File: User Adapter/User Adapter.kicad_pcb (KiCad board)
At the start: 2 copper layers, 88.9 x 27.9 mm, 44 parts, among them J1 OHIS_8p8c_Shield, J2 Headphones, J3 Microphone, J4 PTT, J5 Dynamic Mic Bypass, J6 HP or CTIA, Q1 2N3904, SW1 PTT

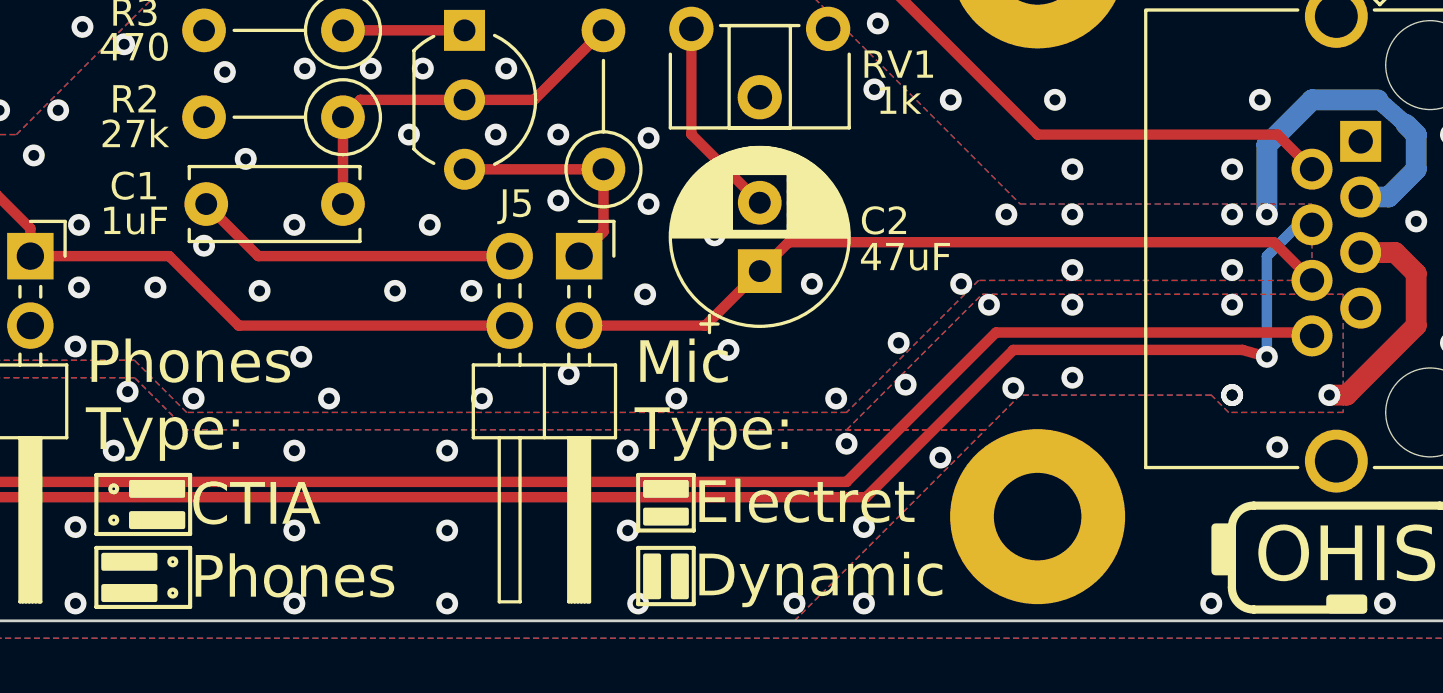
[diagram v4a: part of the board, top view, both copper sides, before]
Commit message: add jumper for mic attenuation. update version on back silkscreen to v1.3
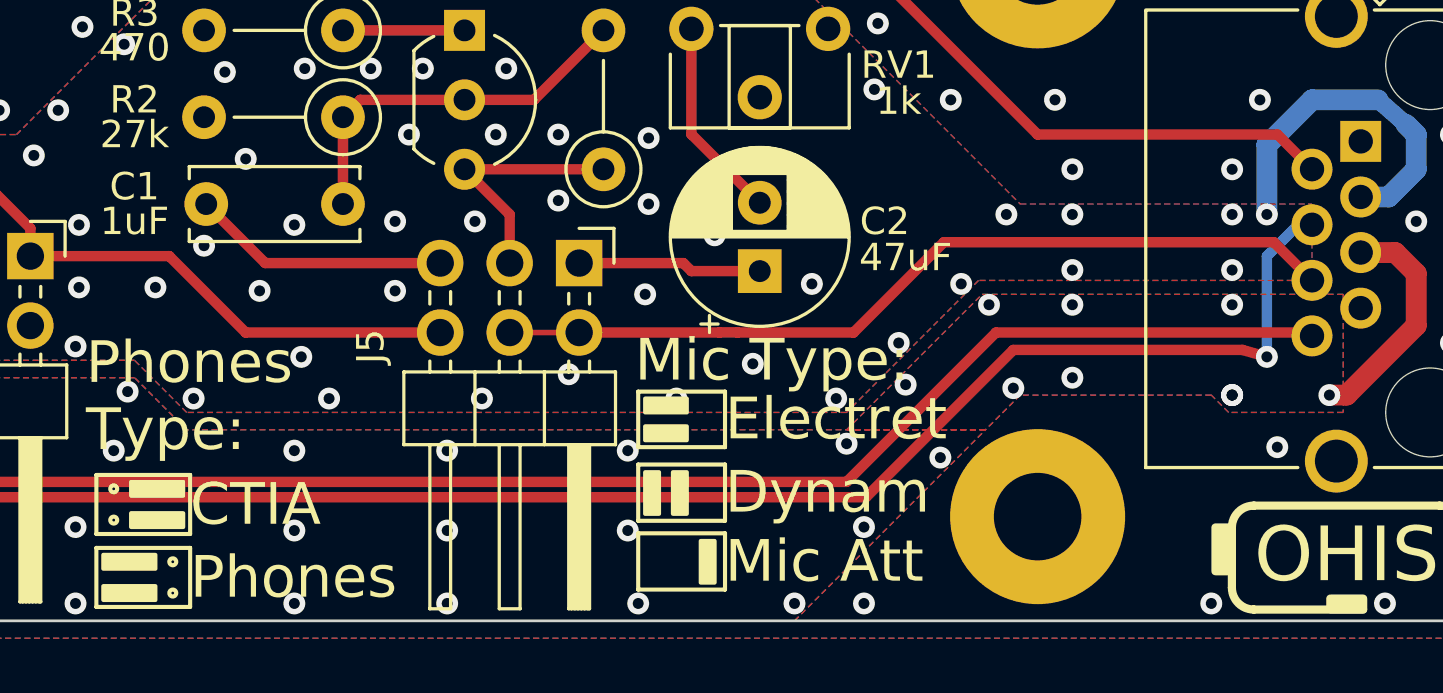
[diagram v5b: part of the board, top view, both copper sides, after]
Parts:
- J5: footprint Connector_PinHeader_2.54mm:PinHeader_2x02_P2.54mm_Horizontal -> Connector_PinHeader_2.54mm:PinHeader_2x03_P2.54mm_Horizontal
- moved J5 0.25 mm to (154.7, 77.1)
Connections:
- C1 pad 1: Net-(J5-Pin_3) -> Net-(J5-Pin_5)
- C2 pad 1: Mic+ -> Net-(J5-Pin_1)
- J5 pad 4: Mic+ 3.5 -> Mic+
- Q1 pad 3: Net-(J5-Pin_1) -> Net-(J5-Pin_3)
- R1 pad 1: Net-(J5-Pin_1) -> Net-(J5-Pin_3)
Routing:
- net Net-(J5-Pin_5): track 0.00 -> 9.45 mm
- net Mic+: track 28.6 -> 31.3 mm
- net Net-(J5-Pin_3): track 11.9 -> 9.19 mm
- net Mic+ 3.5: track 44.2 -> 41.8 mm
- net Net-(J5-Pin_1): track 8.62 -> 6.73 mm
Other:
- board text added: "Dynam"
- board text added: "Mic Att"
- board text added: "OHIS User Adapter v1.3 2024 CC-BY OHIS Working Group"
- board text removed: "Dynamic"
- board text removed: "OHIS User Adapter v1.2a 2024 CC-BY OHIS Working Group"

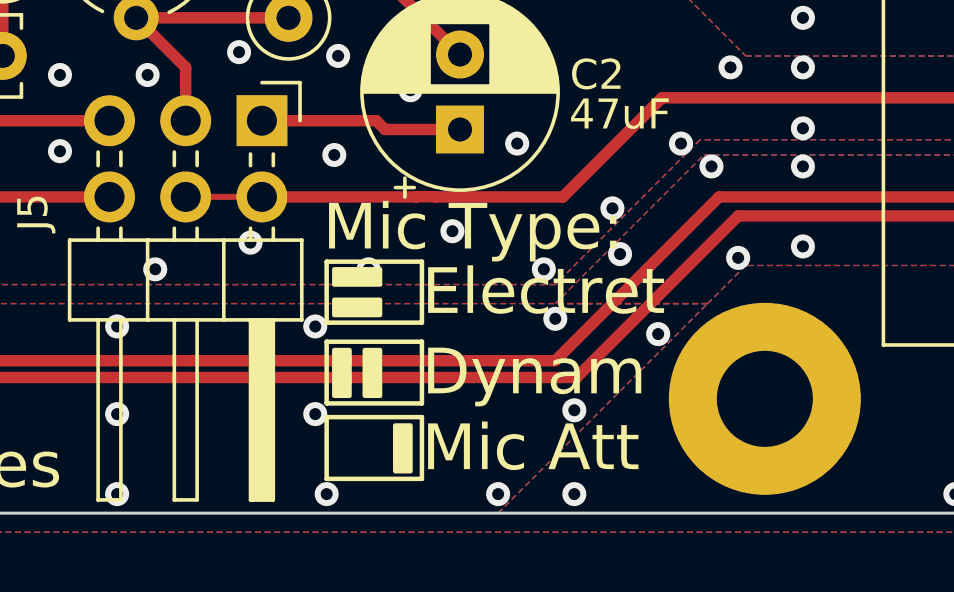
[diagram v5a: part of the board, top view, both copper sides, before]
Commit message: Tweaking a few minor things from the last PR. Added Contributers to README.md
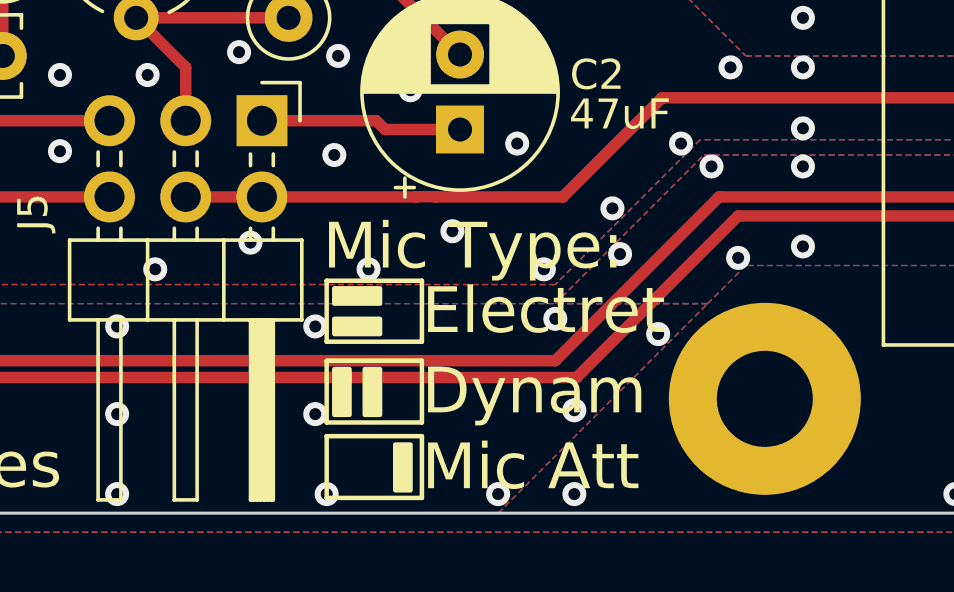
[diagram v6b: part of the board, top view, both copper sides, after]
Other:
- board text added: "OHIS User Adapter v1.3a 2024 CC-BY OHIS Working Group"
- board text removed: "OHIS User Adapter v1.3 2024 CC-BY OHIS Working Group"
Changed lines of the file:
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@@
       (stroke (width 0) (type solid)) (fill solid) (layer "B.SilkS"))
   )
-  (gr_rect (start 159.131 87.249) (end 159.639 88.773)
-    (stroke (width 0.15) (type solid)) (fill solid) (layer "F.SilkS"))
-  (gr_rect (start 157.099 84.7344) (end 157.607 86.2584)
+  (gr_rect (start 159.131 87.884) (end 159.639 89.408)
+    (stroke (width 0.15) (type solid)) (fill solid) (layer "F.SilkS"))
+  (gr_rect (start 157.099 85.3694) (end 157.607 86.8934)
     (stroke (width 0.15) (type solid)) (fill solid) (layer "F.SilkS"))
   (gr_rect (start 137.287 87.757) (end 139.192 88.265)
     (stroke (width 0.15) (type solid)) (fill solid) (layer "F.SilkS"))
-  (gr_rect (start 156.845 84.455) (end 160.02 86.5124)
-    (stroke (width 0.15) (type default)) (fill none) (layer "F.SilkS"))
-  (gr_rect (start 156.845 81.788) (end 160.02 83.82)
-    (stroke (width 0.15) (type default)) (fill none) (layer "F.SilkS"))
-  (gr_rect (start 157.099 83.058) (end 158.623 83.566)
+  (gr_rect (start 156.845 85.09) (end 160.02 87.1474)
+    (stroke (width 0.15) (type default)) (fill none) (layer "F.SilkS"))
+  (gr_rect (start 156.845 82.423) (end 160.02 84.455)
+    (stroke (width 0.15) (type default)) (fill none) (layer "F.SilkS"))
+  (gr_rect (start 157.099 83.693) (end 158.623 84.201)
     (stroke (width 0.15) (type solid)) (fill solid) (layer "F.SilkS"))
   (gr_rect (start 137.287 88.9) (end 139.192 89.408)
@@
   (gr_rect (start 138.303 85.09) (end 140.208 85.598)
     (stroke (width 0.15) (type solid)) (fill solid) (layer "F.SilkS"))
-  (gr_rect (start 156.845 86.9696) (end 160.02 89.027)
+  (gr_rect (start 156.845 87.6046) (end 160.02 89.662)
     (stroke (width 0.15) (type default)) (fill none) (layer "F.SilkS"))
   (gr_circle (center 137.668 86.487) (end 137.668 86.614)
@@
   (gr_circle (center 139.827 88.011) (end 139.827 87.884)
     (stroke (width 0.15) (type default)) (fill none) (layer "F.SilkS"))
-  (gr_rect (start 158.115 84.7344) (end 158.623 86.2584)
+  (gr_rect (start 158.115 85.3694) (end 158.623 86.8934)
     (stroke (width 0.15) (type solid)) (fill solid) (layer "F.SilkS"))
   (gr_rect (start 137.033 87.503) (end 140.462 89.662)
@@
   (gr_rect (start 137.033 84.836) (end 140.462 86.995)
     (stroke (width 0.15) (type default)) (fill none) (layer "F.SilkS"))
-  (gr_rect (start 157.099 82.042) (end 158.623 82.55)
+  (gr_rect (start 157.099 82.677) (end 158.623 83.185)
     (stroke (width 0.15) (type solid)) (fill solid) (layer "F.SilkS"))
   (gr_rect (start 101.6 62.23) (end 190.5 90.17)
@@
     (effects (font (size 1.27 1.27) (thickness 0.1905)) (justify left mirror))
   )
-  (gr_text "OHIS User Adapter v1.3\n2024 CC-BY OHIS Working Group" (at 166.116 85.852) (layer "B.SilkS")
+  (gr_text "OHIS User Adapter v1.3a\n2024 CC-BY OHIS Working Group" (at 166.116 85.852) (layer "B.SilkS")
     (effects (font (size 1.27 1.016) (thickness 0.1905)) (justify left bottom mirror))
   )
@@
     (effects (font (size 1 1) (thickness 0.15)) (justify left bottom mirror))
   )
-  (gr_text "Mic Type:" (at 156.718 81.534) (layer "F.SilkS")
+  (gr_text "Mic Type:" (at 156.718 82.169) (layer "F.SilkS")
     (effects (font (size 1.524 1.524) (thickness 0.2032)) (justify left bottom))
   )
@@
     (effects (font (size 1 1) (thickness 0.15)))
   )
-  (gr_text "Mic Att" (at 160.02 87.9983) (layer "F.SilkS")
+  (gr_text "Mic Att" (at 160.02 88.6333) (layer "F.SilkS")
     (effects (font (size 1.524 1.524) (thickness 0.2032)) (justify left))
   )
@@
     (effects (font (size 1 1) (thickness 0.15)))
   )
-  (gr_text "Dynam" (at 160.02 85.471) (layer "F.SilkS")
+  (gr_text "Dynam" (at 160.02 86.106) (layer "F.SilkS")
     (effects (font (size 1.524 1.524) (thickness 0.2032)) (justify left))
   )
@@
     (effects (font (size 1 1) (thickness 0.15)) (justify bottom))
   )
-  (gr_text "Electret" (at 160.02 82.7913) (layer "F.SilkS")
+  (gr_text "Electret" (at 160.02 83.4263) (layer "F.SilkS")
     (effects (font (size 1.524 1.524) (thickness 0.2032)) (justify left))
   )
@@
     (pts (xy 101.6 76.2) (xy 101.6 85.725))
     (height 3.81)
-    (gr_text "9.5250 mm" (at 96.64 80.9625 90) (layer "Dwgs.User")
+    (gr_text "0.3750 in" (at 96.64 80.9625 90) (layer "Dwgs.User")
       (effects (font (size 1 1) (thickness 0.15)))
     )
@@
     (pts (xy 171.45 66.04) (xy 171.45 86.36))
     (height -26.67)
-    (gr_text "20.3200 mm" (at 196.97 76.2 90) (layer "Dwgs.User")
+    (gr_text "0.8000 in" (at 196.97 76.2 90) (layer "Dwgs.User")
       (effects (font (size 1 1) (thickness 0.15)))
     )
@@
     (pts (xy 120.65 66.04) (xy 101.6 66.04))
     (height 6.35)
-    (gr_text "19.0500 mm" (at 111.125 58.54) (layer "Dwgs.User")
+    (gr_text "0.7500 in" (at 111.125 58.54) (layer "Dwgs.User")
       (effects (font (size 1 1) (thickness 0.15)))
     )
@@
     (pts (xy 190.5 62.23) (xy 190.5 90.17))
     (height -10.795)
-    (gr_text "27.9400 mm" (at 200.145 76.2 90) (layer "Dwgs.User")
+    (gr_text "1.1000 in" (at 200.145 76.2 90) (layer "Dwgs.User")
       (effects (font (size 1 1) (thickness 0.15)))
     )
@@
     (pts (xy 121.285 76.2) (xy 101.6 76.2))
     (height 21.59)
-    (gr_text "19.6850 mm" (at 111.4425 53.46) (layer "Dwgs.User")
+    (gr_text "0.7750 in" (at 111.4425 53.46) (layer "Dwgs.User")
       (effects (font (size 1 1) (thickness 0.15)))
     )
@@
     (pts (xy 101.6 62.23) (xy 190.5 62.23))
     (height -5.715)
-    (gr_text "88.9000 mm" (at 146.05 55.365) (layer "Dwgs.User")
+    (gr_text "3.5000 in" (at 146.05 55.365) (layer "Dwgs.User")
       (effects (font (size 1 1) (thickness 0.15)))
     )
@@
     (pts (xy 101.6 76.2) (xy 101.6 66.675))
     (height -3.81)
-    (gr_text "9.5250 mm" (at 96.64 71.4375 90) (layer "Dwgs.User")
+    (gr_text "0.3750 in" (at 96.64 71.4375 90) (layer "Dwgs.User")
       (effects (font (size 1 1) (thickness 0.15)))
     )
@@
     (pts (xy 120.65 66.04) (xy 171.45 66.04))
     (height -6.35)
-    (gr_text "50.8000 mm" (at 146.05 58.54) (layer "Dwgs.User")
+    (gr_text "2.0000 in" (at 146.05 58.54) (layer "Dwgs.User")
       (effects (font (size 1 1) (thickness 0.15)))
     )
@@
   (segment (start 154.686 79.629) (end 154.7288 79.5862) (width 0.2) (layer "F.Cu") (net 7))
   (segment (start 160.465241 79.6227) (end 159.828759 79.6227) (width 0.381) (layer "F.Cu") (net 7))
-  (segment (start 152.146 79.629) (end 154.686 79.629) (width 0.2) (layer "F.Cu") (net 7))
+  (segment (start 152.146 79.629) (end 154.686 79.629) (width 0.381) (layer "F.Cu") (net 7))
   (via (at 168.275 71.12) (size 0.8) (drill 0.4) (layers "F.Cu" "B.Cu") (free) (net 8))
   (via (at 165.608 68.326) (size 0.8) (drill 0.4) (layers "F.Cu" "B.Cu") (free) (net 8))
